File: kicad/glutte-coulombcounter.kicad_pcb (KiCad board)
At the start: 2 copper layers, 85 x 50 mm, 59 parts, among them J1 12V, J2 Measure, J3 I2C, J4 AVR-ISP-6, J5 DB9_Female, U1 DS18B20, U2 LT1236-5, U3 LT3433, U4 AD8210, U5 LTC2400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

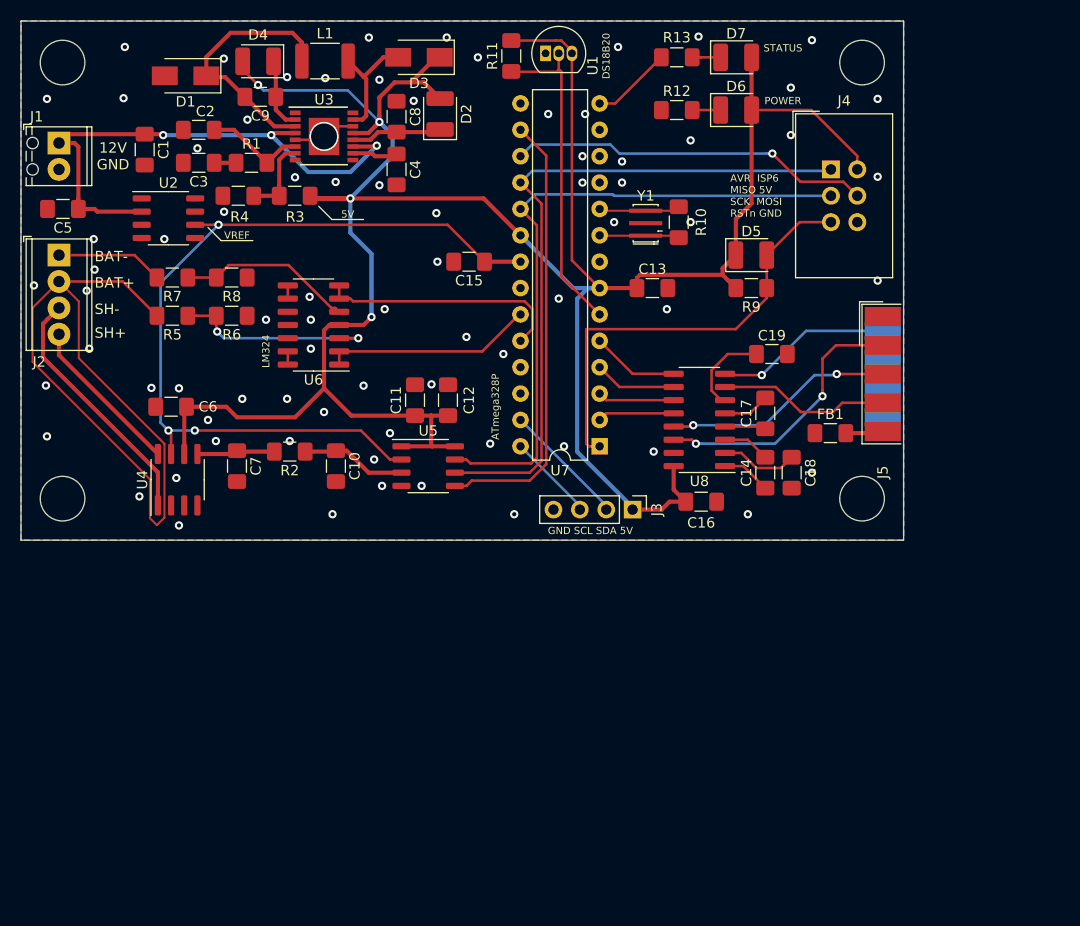
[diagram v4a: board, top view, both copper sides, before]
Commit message: Add relays
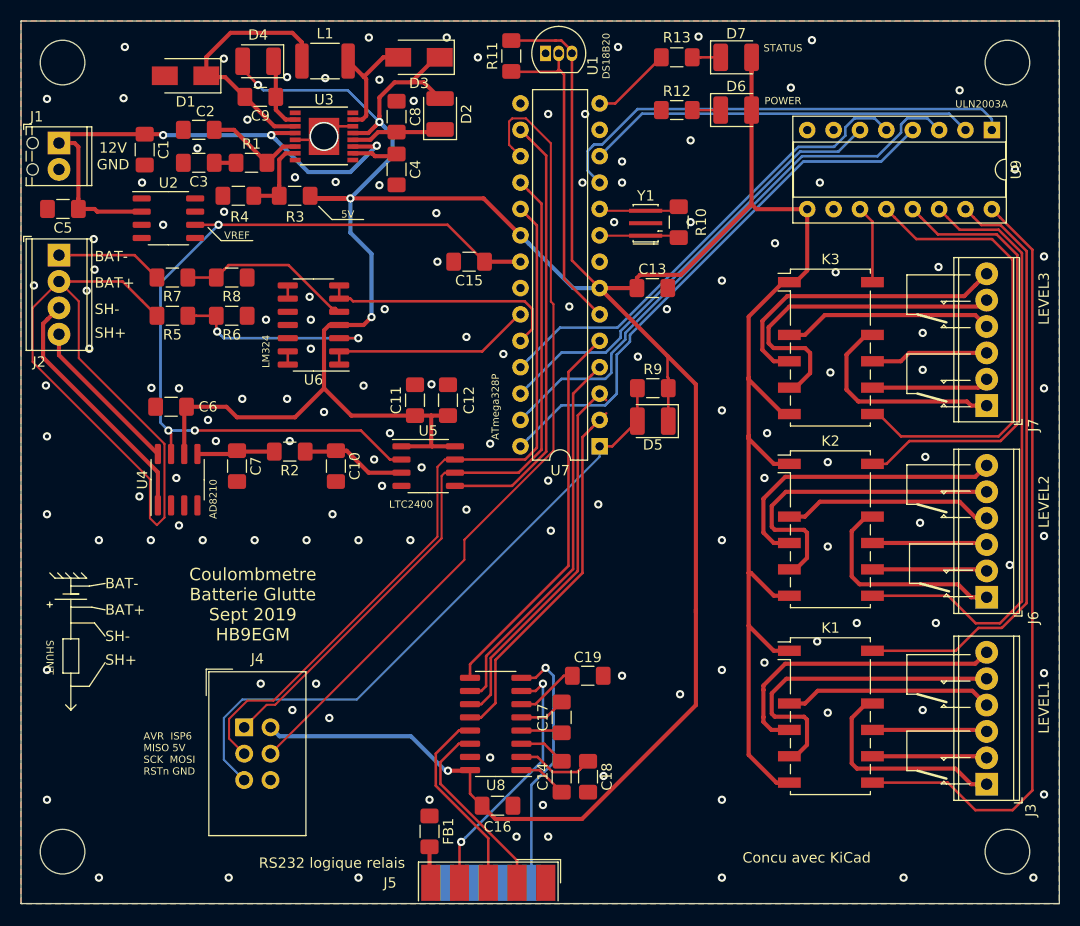
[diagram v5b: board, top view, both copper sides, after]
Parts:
- added J6: K2, TerminalBlock_Phoenix:TerminalBlock_Phoenix_MPT-0,5-6-2.54_1x06_P2.54mm_Horizontal, F.Cu at (123.0, 75.5)
- added J7: K3, TerminalBlock_Phoenix:TerminalBlock_Phoenix_MPT-0,5-6-2.54_1x06_P2.54mm_Horizontal, F.Cu at (123.0, 57.0)
- added K1: G6SK-2F-DC5, Relay_SMD:Relay_DPDT_Omron_G6SK-2F, F.Cu at (108.0, 87.0)
- added K2: G6SK-2F-DC5, Relay_SMD:Relay_DPDT_Omron_G6SK-2F, F.Cu at (108.0, 69.0)
- added K3: G6SK-2F-DC5, Relay_SMD:Relay_DPDT_Omron_G6SK-2F, F.Cu at (108.0, 51.5)
- added U9: ULN2003A, Package_DIP:DIP-16_W7.62mm_Socket, F.Cu at (123.5, 30.5)
- J3: value I2C -> K1; footprint Connector_PinHeader_2.54mm:PinHeader_1x04_P2.54mm_Vertical -> TerminalBlock_Phoenix:TerminalBlock_Phoenix_MPT-0,5-6-2.54_1x06_P2.54mm_Horizontal
- moved J4 78.0 mm to (51.5, 88.0)
- moved J5 62.0 mm to (75.0, 103.0), turned to 0 degrees
- moved FB1 54.4 mm to (69.3, 98.0), turned to 270 degrees
- moved J3 43.2 mm to (123.0, 93.5), turned to 90 degrees
- moved H4 36.8 mm to (125.0, 100.0)
- moved C19 35.7 mm to (84.6, 83.1)
- moved C14 35.2 mm to (82.1, 92.8)
- moved C16 35.2 mm to (75.9, 95.6)
- moved C17 35.2 mm to (82.1, 87.1)
- moved C18 35.2 mm to (84.6, 92.8)
- moved U8 35.2 mm to (75.7, 87.7)
- moved H2 34.0 mm to (34.0, 100.0)
- moved D5 18.6 mm to (90.8, 58.5), turned to 180 degrees
- moved H3 14.0 mm to (125.0, 24.0)
- moved R9 13.5 mm to (90.8, 55.4), turned to 0 degrees
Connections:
- J3 pad 1: +5VA -> Net-(J3-Pad1)
- J3 pad 2: /SDA -> Net-(J3-Pad2)
- J3 pad 3: /SCL -> Net-(J3-Pad3)
- J3 pad 4: GNDA -> Net-(J3-Pad4)
- U7 pad 11: (no net) -> /Relays/K1_RESET
- U7 pad 12: (no net) -> /Relays/K1_SET
- U7 pad 25: (no net) -> /Relays/K3_RESET
- U7 pad 26: (no net) -> /Relays/K3_SET
- U7 pad 27: /SDA -> /Relays/K2_RESET
- U7 pad 28: /SCL -> /Relays/K2_SET
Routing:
- net +5VA: track 256.1 -> 392.2 mm, vias 4 -> 5
- net Net-(K1-Pad7): track 0.00 -> 74.9 mm
- net Net-(K2-Pad7): track 0.00 -> 59.6 mm
- net Net-(K1-Pad12): track 0.00 -> 58.2 mm
- net /Relays/K2_RESET: track 0.00 -> 54.7 mm
- net /Relays/K2_SET: track 0.00 -> 53.0 mm
- net /Relays/K3_RESET: track 0.00 -> 46.1 mm
- net /Relays/K1_RESET: track 0.00 -> 45.6 mm
- net Net-(K3-Pad7): track 0.00 -> 44.8 mm
- net /MOSI: track 34.9 -> 79.1 mm, vias 1 -> 0
- net Net-(K2-Pad12): track 0.00 -> 43.7 mm
- net /Relays/K3_SET: track 0.00 -> 43.6 mm
- net /Relays/K1_SET: track 0.00 -> 37.6 mm
- net Net-(J7-Pad5): track 0.00 -> 32.5 mm
- net Net-(J6-Pad5): track 0.00 -> 31.5 mm
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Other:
- board size 85 x 50 mm -> 100 x 85 mm
- net class Relay added: clearance 0.4, trace_width 0.4, via_dia 1, via_drill 0.6
- board text added: "AD8210"
- board text added: "Coulombmetre Batterie Glutte Sept 2019 HB9EGM"
- board text added: "LEVEL1"
- board text added: "LEVEL2"
- board text added: "LEVEL3"
- board text added: "LTC2400"
- board text added: "RS232 logique relais"
- board text added: "ULN2003A"
- board text removed: "Coulombmetre Batterie Glutte Aout 2019 HB9EGM"
- board text removed: "GND SCL SDA 5V"

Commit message: Add second UART output for Raspi
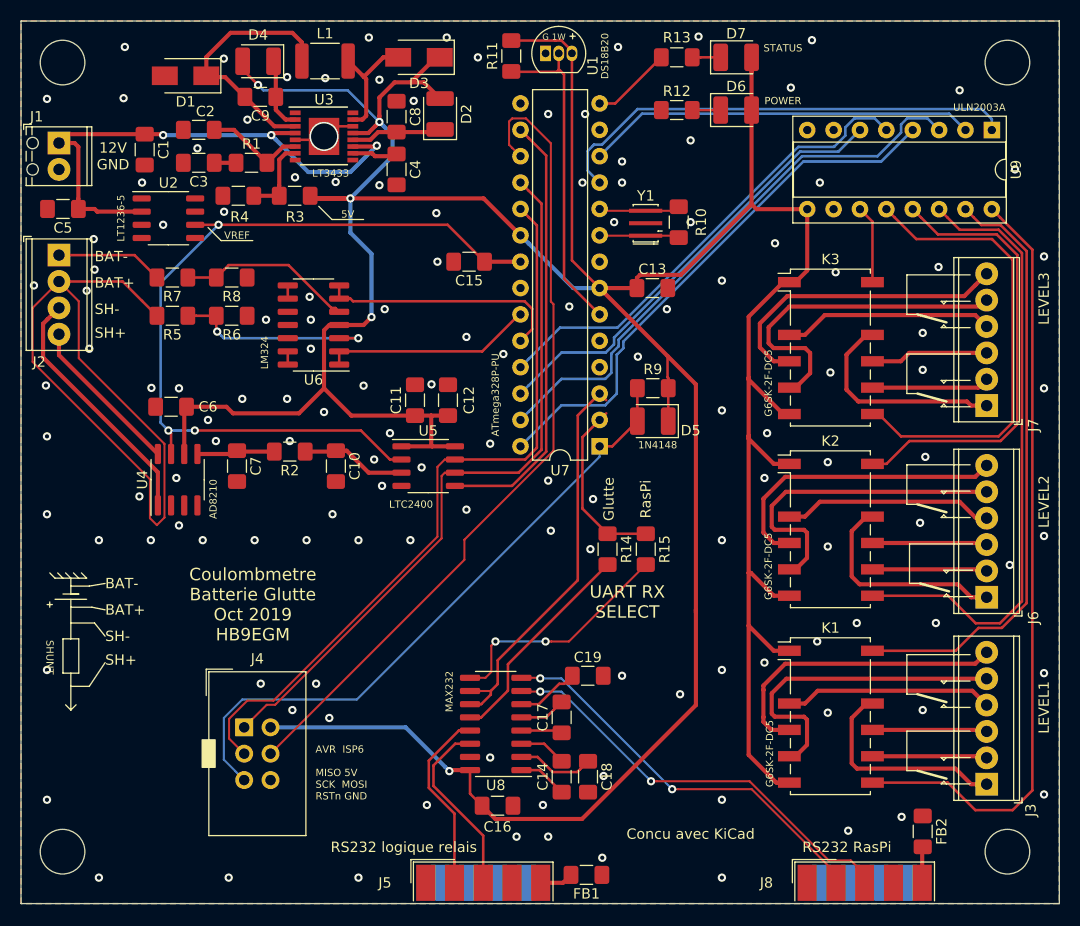
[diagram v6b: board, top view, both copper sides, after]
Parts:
- added FB2: DNF, Resistor_SMD:R_1206_3216Metric_Pad1.42x1.75mm_HandSolder, F.Cu at (116.8, 98.0)
- added J8: Raspi, Connector_Dsub:DSUB-9_Male_EdgeMount_P2.77mm, F.Cu at (111.3, 103.0)
- added R14: 0R, Resistor_SMD:R_1206_3216Metric_Pad1.42x1.75mm_HandSolder, F.Cu at (86.5, 70.9)
- added R15: DNF, Resistor_SMD:R_1206_3216Metric_Pad1.42x1.75mm_HandSolder, F.Cu at (90.2, 70.9)
- J5: value DB9_Female -> Glutte; footprint Connector_Dsub:DSUB-9_Female_EdgeMount_P2.77mm -> Connector_Dsub:DSUB-9_Male_EdgeMount_P2.77mm
- moved FB1 15.7 mm to (84.5, 102.2), turned to 180 degrees
- moved J5 0.49 mm to (74.5, 103.0)
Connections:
- J5 pad 4: Net-(J5-Pad4) -> (no net)
- J5 pad 6: Net-(J5-Pad6) -> (no net)
- U7 pad 4: /DTR -> (no net)
- U7 pad 5: /DSR -> (no net)
- U8 pad 10: /DTR -> /TXD
- U8 pad 12: /RXD -> Net-(R14-Pad2)
- U8 pad 13: Net-(J5-Pad3) -> Net-(J5-Pad2)
- U8 pad 14: Net-(J5-Pad2) -> Net-(J5-Pad3)
- U8 pad 7: Net-(J5-Pad4) -> Net-(J8-Pad3)
- U8 pad 8: Net-(J5-Pad6) -> Net-(J8-Pad2)
- U8 pad 9: /DSR -> Net-(R15-Pad2)
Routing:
- net Net-(J8-Pad3): track 0.00 -> 41.2 mm, vias 0 -> 2
- net Net-(J8-Pad2): track 0.00 -> 39.0 mm, vias 0 -> 2
- net /DSR: track 37.6 -> 0.00 mm
- net /DTR: track 37.0 -> 0.00 mm
- net Net-(J5-Pad4): track 24.9 -> 0.00 mm, vias 2 -> 0
- net Net-(J5-Pad6): track 24.6 -> 0.00 mm, vias 1 -> 0
- net Net-(R15-Pad2): track 0.00 -> 22.9 mm, vias 0 -> 2
- net Net-(R14-Pad2): track 0.00 -> 20.8 mm
- net /RXD: track 35.3 -> 17.2 mm
- net Net-(FB2-Pad2): track 0.00 -> 3.49 mm
- net /TXD: track 36.6 -> 38.6 mm
- net Net-(J5-Pad3): track 18.8 -> 17.7 mm
- net GNDA: vias 134 -> 135
- net (no net): vias 0 -> 1
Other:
- board text added: "1W"
- board text added: "Coulombmetre Batterie Glutte Oct 2019 HB9EGM"
- board text added: "G"
- board text added: "Glutte"
- board text added: "RS232 RasPi"
- board text added: "RasPi"
- board text added: "UART RX SELECT"
- board text removed: "ATmega328P"
- board text removed: "Coulombmetre Batterie Glutte Sept 2019 HB9EGM"
- board text removed: "DS18B20"
- board text removed: "LM324"
- board text removed: "ULN2003A"

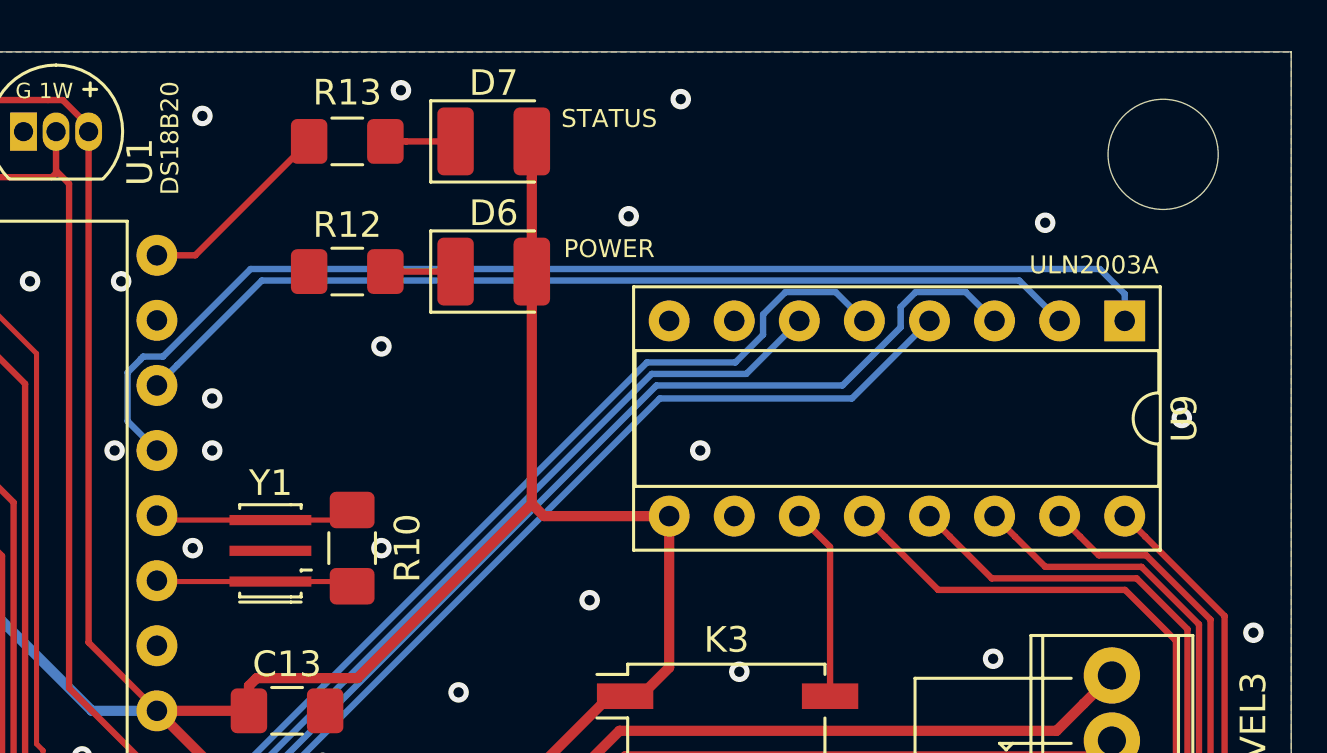
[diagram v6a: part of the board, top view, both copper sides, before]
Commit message: Add resistor network on relay control signals
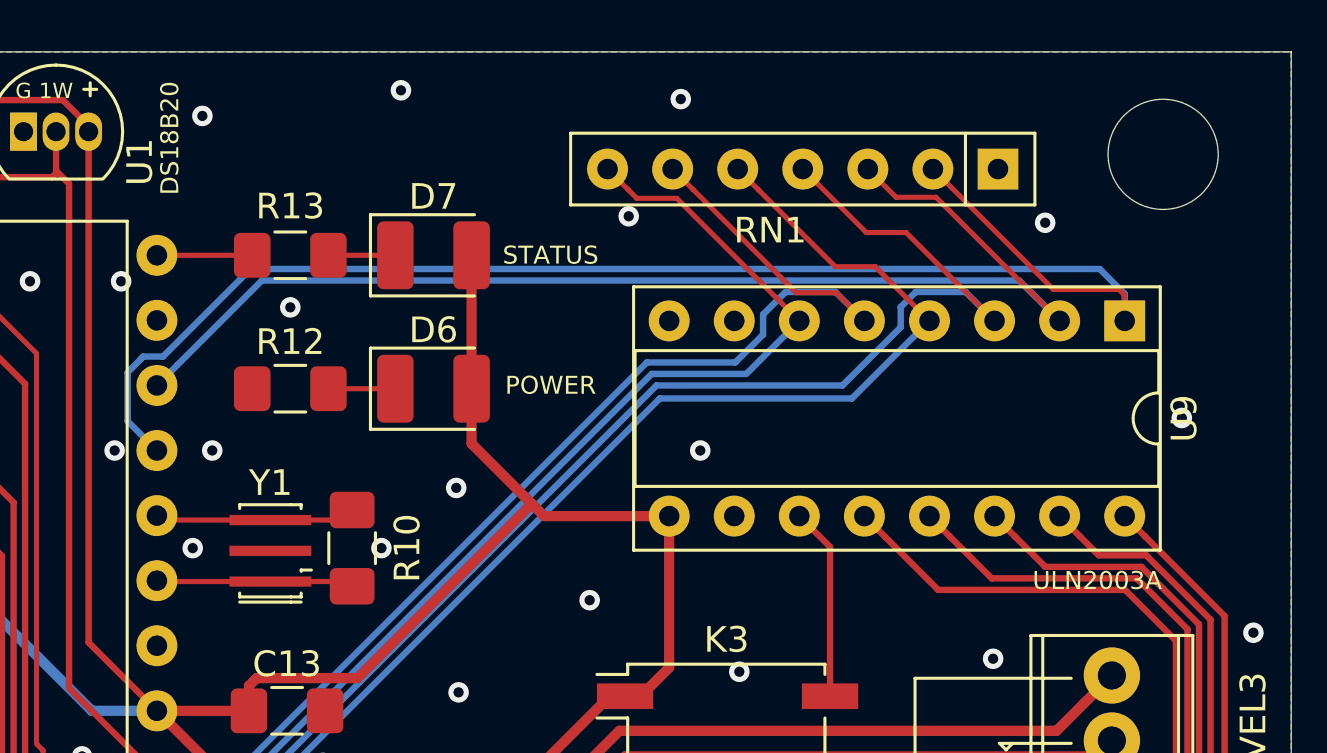
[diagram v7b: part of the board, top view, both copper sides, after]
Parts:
- added RN1: 470R, Resistor_THT:R_Array_SIP7, F.Cu at (118.6, 24.6)
- moved D6 5.14 mm to (96.5, 33.1)
- moved R12 5.08 mm to (90.9, 33.1)
- moved D7 5.03 mm to (96.5, 27.9)
- moved R13 4.97 mm to (90.9, 27.9)
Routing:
- net /Relays/K1_RESET: track 45.6 -> 56.1 mm
- net /Relays/K3_RESET: track 46.1 -> 56.0 mm
- net /Relays/K2_SET: track 53.0 -> 62.9 mm
- net /Relays/K2_RESET: track 54.7 -> 64.7 mm
- net /Relays/K3_SET: track 43.6 -> 53.5 mm
- net /Relays/K1_SET: track 37.6 -> 47.5 mm
- net /STATUS: track 7.78 -> 3.72 mm
- net +5VA: track 391.9 -> 388.4 mm
